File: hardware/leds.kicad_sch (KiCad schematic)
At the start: 20 parts

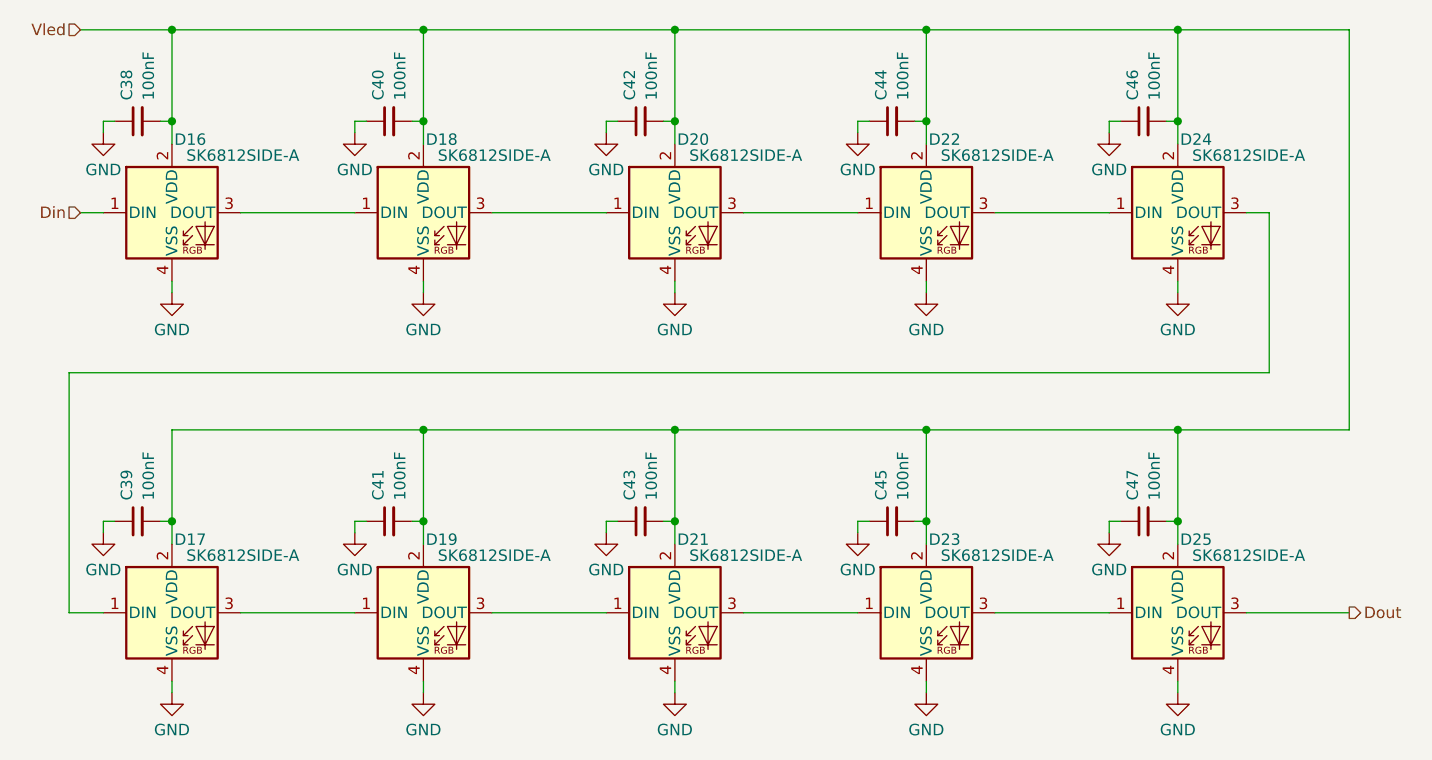
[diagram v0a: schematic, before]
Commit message: rev 0.4 move button next to ethernet jack, kicad v9
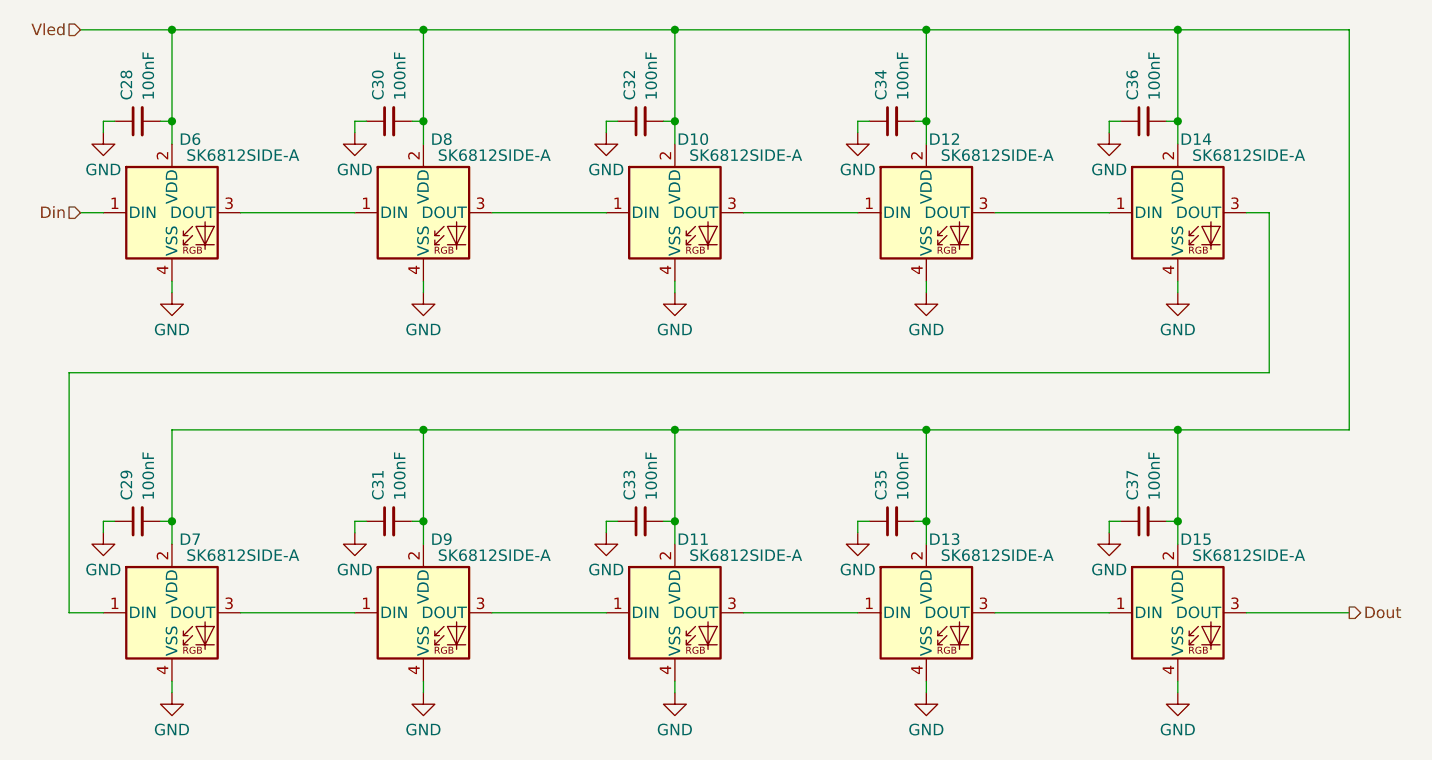
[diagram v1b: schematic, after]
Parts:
- renumbered C38 to C28, C39 to C29, C40 to C30, C41 to C31, C42 to C32, C43 to C33, C44 to C34, C45 to C35, C46 to C36, C47 to C37, D20 to D10, D21 to D11, D22 to D12, D23 to D13, D24 to D14, D25 to D15, D16 to D6, D17 to D7, D18 to D8, D19 to D9
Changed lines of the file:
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@@
 (kicad_sch
-	(version 20231120)
+	(version 20250114)
 	(generator "eeschema")
-	(generator_version "8.0")
+	(generator_version "9.0")
 	(paper "A4")
 	(junction
@@
 		(on_board yes)
 		(dnp no)
-		(property "Reference" "D24"
+		(property "Reference" "D14"
 			(at 186.182 75.692 0)
 			(effects
@@
 		(dnp no)
 		(fields_autoplaced yes)
-		(property "Reference" "#PWR078"
+		(property "Reference" "#PWR058"
 			(at 100.33 99.06 0)
 			(effects
@@
 		(dnp no)
 		(fields_autoplaced yes)
-		(property "Reference" "#PWR074"
+		(property "Reference" "#PWR054"
 			(at 72.39 99.06 0)
 			(effects
@@
 		(dnp no)
 		(fields_autoplaced yes)
-		(property "Reference" "#PWR087"
+		(property "Reference" "#PWR067"
 			(at 156.21 143.51 0)
 			(effects
@@
 		(dnp no)
 		(fields_autoplaced yes)
-		(property "Reference" "#PWR073"
+		(property "Reference" "#PWR053"
 			(at 64.77 125.73 0)
 			(effects
@@
 		(on_board yes)
 		(dnp no)
-		(property "Reference" "C43"
+		(property "Reference" "C33"
 			(at 123.2541 115.7859 0)
 			(effects
@@
 		(on_board yes)
 		(dnp no)
-		(property "Reference" "D23"
+		(property "Reference" "D13"
 			(at 158.242 120.142 0)
 			(effects
@@
 		(dnp no)
 		(fields_autoplaced yes)
-		(property "Reference" "#PWR084"
+		(property "Reference" "#PWR064"
 			(at 148.59 81.28 0)
 			(effects
@@
 		(on_board yes)
 		(dnp no)
-		(property "Reference" "C41"
+		(property "Reference" "C31"
 			(at 95.3141 115.7859 0)
 			(effects
@@
 		(dnp no)
 		(fields_autoplaced yes)
-		(property "Reference" "#PWR072"
+		(property "Reference" "#PWR052"
 			(at 64.77 81.28 0)
 			(effects
@@
 		(on_board yes)
 		(dnp no)
-		(property "Reference" "D19"
+		(property "Reference" "D9"
 			(at 102.362 120.142 0)
 			(effects
@@
 		(on_board yes)
 		(dnp no)
-		(property "Reference" "C46"
+		(property "Reference" "C36"
 			(at 179.1341 71.3359 0)
 			(effects
@@
 		(dnp no)
 		(fields_autoplaced yes)
-		(property "Reference" "#PWR082"
+		(property "Reference" "#PWR062"
 			(at 128.27 99.06 0)
 			(effects
@@
 		(on_board yes)
 		(dnp no)
-		(property "Reference" "C47"
+		(property "Reference" "C37"
 			(at 179.1341 115.7859 0)
 			(effects
@@
 		(on_board yes)
 		(dnp no)
-		(property "Reference" "D18"
+		(property "Reference" "D8"
 			(at 102.362 75.692 0)
 			(effects
@@
 		(dnp no)
 		(fields_autoplaced yes)
-		(property "Reference" "#PWR081"
+		(property "Reference" "#PWR061"
 			(at 120.65 125.73 0)
 			(effects
@@
 		(dnp no)
 		(fields_autoplaced yes)
-		(property "Reference" "#PWR076"
+		(property "Reference" "#PWR056"
 			(at 92.71 81.28 0)
 			(effects
@@
 		(on_board yes)
 		(dnp no)
-		(property "Reference" "C38"
+		(property "Reference" "C28"
 			(at 67.3741 71.3359 0)
 			(effects
@@
 		(on_board yes)
 		(dnp no)
-		(property "Reference" "C42"
+		(property "Reference" "C32"
 			(at 123.2541 71.3359 0)
 			(effects
@@
 		(dnp no)
 		(fields_autoplaced yes)
-		(property "Reference" "#PWR090"
+		(property "Reference" "#PWR070"
 			(at 184.15 99.06 0)
 			(effects
@@
 		(on_board yes)
 		(dnp no)
-		(property "Reference" "C44"
+		(property "Reference" "C34"
 			(at 151.1941 71.3359 0)
 			(effects
@@
 		(dnp no)
 		(fields_autoplaced yes)
-		(property "Reference" "#PWR091"
+		(property "Reference" "#PWR071"
 			(at 184.15 143.51 0)
 			(effects
@@
 		(dnp no)
 		(fields_autoplaced yes)
-		(property "Reference" "#PWR077"
+		(property "Reference" "#PWR057"
 			(at 92.71 125.73 0)
 			(effects
@@
 		(on_board yes)
 		(dnp no)
-		(property "Reference" "D22"
+		(property "Reference" "D12"
 			(at 158.242 75.692 0)
 			(effects
@@
 		(on_board yes)
 		(dnp no)
-		(property "Reference" "D16"
+		(property "Reference" "D6"
 			(at 74.422 75.692 0)
 			(effects
@@
 		(dnp no)
 		(fields_autoplaced yes)
-		(property "Reference" "#PWR075"
+		(property "Reference" "#PWR055"
 			(at 72.39 143.51 0)
 			(effects
@@
 		(dnp no)
 		(fields_autoplaced yes)
-		(property "Reference" "#PWR088"
+		(property "Reference" "#PWR068"
 			(at 176.53 81.28 0)
 			(effects
@@
 		(dnp no)
 		(fields_autoplaced yes)
-		(property "Reference" "#PWR089"
+		(property "Reference" "#PWR069"
 			(at 176.53 125.73 0)
 			(effects
@@
 		(dnp no)
 		(fields_autoplaced yes)
-		(property "Reference" "#PWR086"
+		(property "Reference" "#PWR066"
 			(at 156.21 99.06 0)
 			(effects
@@
 		(on_board yes)
 		(dnp no)
-		(property "Reference" "C45"
+		(property "Reference" "C35"
 			(at 151.1941 115.7859 0)
 			(effects
@@
 		(dnp no)
 		(fields_autoplaced yes)
-		(property "Reference" "#PWR080"
+		(property "Reference" "#PWR060"
 			(at 120.65 81.28 0)
 			(effects
@@
 		(on_board yes)
 		(dnp no)
-		(property "Reference" "C39"
+		(property "Reference" "C29"
 			(at 67.3741 115.7859 0)
 			(effects
@@
 		(dnp no)
 		(fields_autoplaced yes)
-		(property "Reference" "#PWR085"
+		(property "Reference" "#PWR065"
 			(at 148.59 125.73 0)
 			(effects
@@
 		(on_board yes)
 		(dnp no)
-		(property "Reference" "D21"
+		(property "Reference" "D11"
 			(at 130.302 120.142 0)
 			(effects
@@
 		(on_board yes)
 		(dnp no)
-		(property "Reference" "D17"
+		(property "Reference" "D7"
 			(at 74.422 120.142 0)
 			(effects
@@
 		(on_board yes)
 		(dnp no)
-		(property "Reference" "C40"
+		(property "Reference" "C30"
 			(at 95.3141 71.3359 0)
 			(effects
@@
 		(dnp no)
 		(fields_autoplaced yes)
-		(property "Reference" "#PWR079"
+		(property "Reference" "#PWR059"
 			(at 100.33 143.51 0)
 			(effects
@@
 		(on_board yes)
 		(dnp no)
-		(property "Reference" "D20"
+		(property "Reference" "D10"
 			(at 130.302 75.692 0)
 			(effects
@@
 		(on_board yes)
 		(dnp no)
-		(property "Reference" "D25"
+		(property "Reference" "D15"
 			(at 186.182 120.142 0)
 			(effects
@@
 		(dnp no)
 		(fields_autoplaced yes)
-		(property "Reference" "#PWR083"
+		(property "Reference" "#PWR063"
 			(at 128.27 143.51 0)
 			(effects
